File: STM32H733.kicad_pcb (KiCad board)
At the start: 4 copper layers, 38.3 x 38.3 mm, 84 parts, among them IC1 AT7456E, J1 USB, J2 DJI, J3 SWD, J4 CAM, J6 VTX, J7 GPS, J8 ESC, J9 ELRS, U1 STM32H733VGTx, U2 ICM-42688-P, U3 TLV75733PDBV, U4 TJA1051TK-3, U5 BMP280, U6 W25Q128JVP, U7 LMR51430, U8 LMR51430, Y1 Resonator_Small, Y2 27MHz

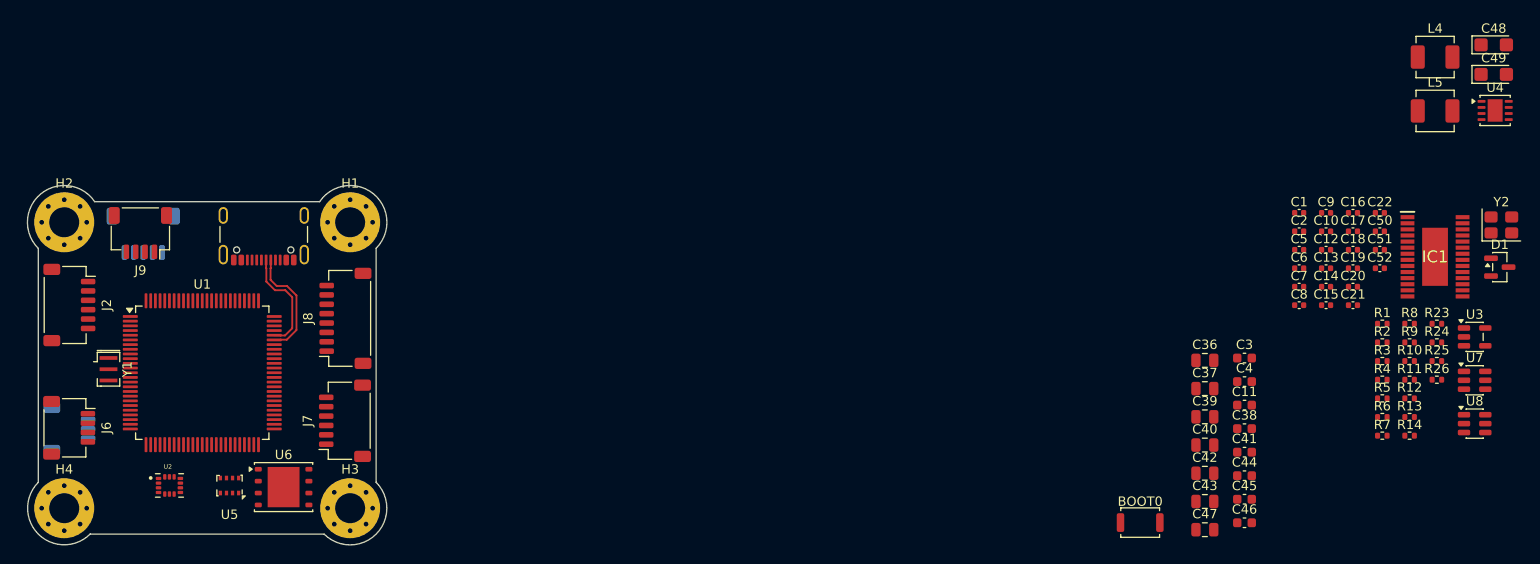
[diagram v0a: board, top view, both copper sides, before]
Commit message: New Layout designed
Signed-off-by: Asraful Islam Taj <asraful.islam.taj@gmail.com>
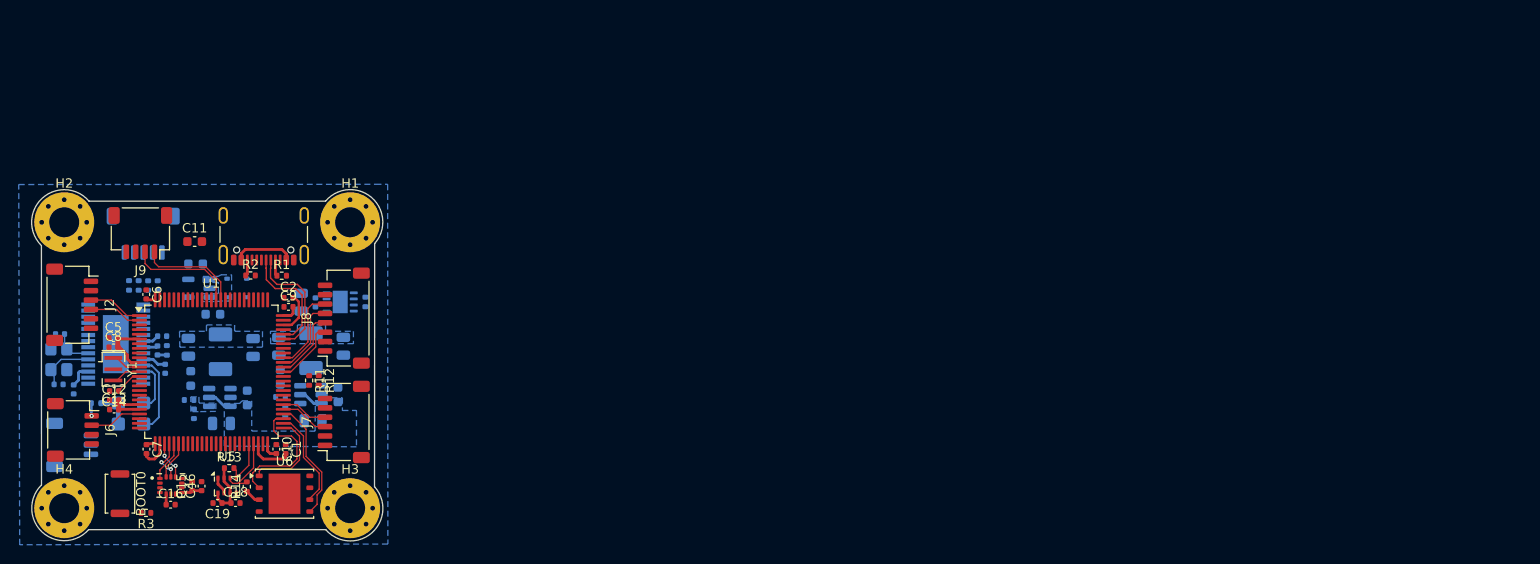
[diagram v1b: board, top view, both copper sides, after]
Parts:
- added D2: 1N5819WS, Diode_SMD:D_SOD-323, B.Cu at (140.4, 67.0)
- C17, C20, C21, C22, C3, C36, C37, C38, C39, C4, C40, C41, C42, C43, C44, C45, C47, C48, C49, C50, C51, C52, IC1, L4, L5, R10, R23, R24, R25, R26, R4, R5, R6, R7, R8, R9, U3, U4, U7, U8, Y2: moved to B.Cu
- C46: footprint Capacitor_SMD:C_0603_1608Metric -> Capacitor_SMD:C_0402_1005Metric
- D1: value BAT54C -> 1N5819WS; footprint Package_TO_SOT_SMD:SOT-23 -> Diode_SMD:D_SOD-323; moved to B.Cu
- moved Y2 154.5 mm to (121.4, 75.6), turned to 90 degrees
- moved C48 150.3 mm to (129.1, 80.3), turned to 180 degrees
- moved C49 150.1 mm to (129.1, 82.5), turned to 180 degrees
- moved C51 141.7 mm to (121.4, 78.3)
- moved IC1 141.0 mm to (127.5, 74.0)
- moved C52 141.0 mm to (121.6, 72.9), turned to 180 degrees
- moved R5 137.2 mm to (125.4, 80.3), turned to 180 degrees
- moved R10 136.8 mm to (128.9, 67.7), turned to -90 degrees
- moved C21 136.8 mm to (123.0, 78.8), turned to 90 degrees
- moved U3 136.2 mm to (136.4, 68.0), turned to 180 degrees
- moved R9 135.7 mm to (129.9, 67.7), turned to -90 degrees
- moved D1 134.8 mm to (140.4, 69.0)
- moved R8 134.6 mm to (130.9, 67.8), turned to -90 degrees
- moved U8 133.9 mm to (138.6, 79.7), turned to 180 degrees
- moved R25 133.2 mm to (135.3, 80.0)
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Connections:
- net /VBAT renamed VBAT
- C3 pad 1: Net-(U3-EN) -> Net-(D1-K)
- D1 pad 1: +5VUSB -> Net-(D1-K)
- J9 pad 1: /RC_USART2_RX -> /RC_USART2_TX
- J9 pad 2: /RC_USART2_TX -> /RC_USART2_RX
- U1 pad 55: /GPS_USART1_TX -> /GPS_USART1_RX
- U1 pad 56: /GPS_USART1_RX -> /GPS_USART1_TX
- U3 pad 1: Net-(U3-EN) -> Net-(D1-K)
- U3 pad 3: Net-(U3-EN) -> Net-(D1-K)
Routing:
- net +3.3V: track 0.00 -> 25.6 mm
- net /FLASH_MISO: track 0.00 -> 14.2 mm
- net /FLASH_MOSI: track 0.00 -> 13.1 mm
- net /RC_USART2_RX: track 0.00 -> 11.6 mm
- net /RC_USART2_TX: track 0.00 -> 11.0 mm
- net /FLASH_SCK: track 0.00 -> 10.6 mm
- net /FLASH_CS: track 0.00 -> 9.92 mm
- net /TIM8_CH4: track 0.00 -> 8.92 mm
- net Net-(IC1-SAG): track 0.00 -> 8.66 mm
- net /TIM8_CH3: track 0.00 -> 8.31 mm
- net /TIM8_CH2: track 0.00 -> 7.62 mm
- net /BARO_I2C2_SDA: track 0.00 -> 7.16 mm
- net /TIM8_CH1: track 0.00 -> 6.99 mm
- net +B5V: track 0.00 -> 6.90 mm
- net +5VUSB: track 0.00 -> 6.52 mm
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- added copper zone on B.Cu, net +B5V
- added copper zone on B.Cu, net +B9V
- added copper zone on B.Cu, net GND
- added copper zone on B.Cu, net Net-(D1-K)
- added copper zone on B.Cu, net Net-(U8-FB)
- added copper zone on B.Cu, net VBAT
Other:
- board size 38.3 x 38.3 mm -> 37.5 x 37.5 mm
